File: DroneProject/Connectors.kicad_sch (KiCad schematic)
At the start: 7 parts, among them J21 Battery, J22 Debug, J23 UART, J24 Screw_Terminal_01x03, J25 Screw_Terminal_01x03, J26 Screw_Terminal_01x03, J27 Screw_Terminal_01x03

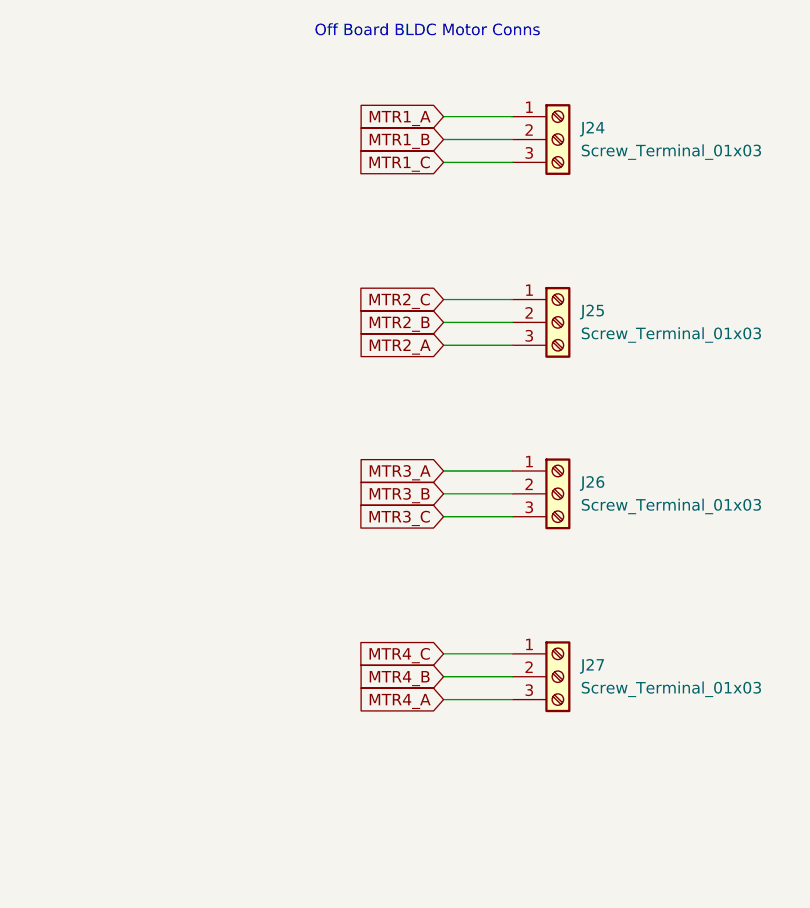
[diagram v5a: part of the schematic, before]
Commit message: Removed C1 and motor controllers from main platform and moved to own project
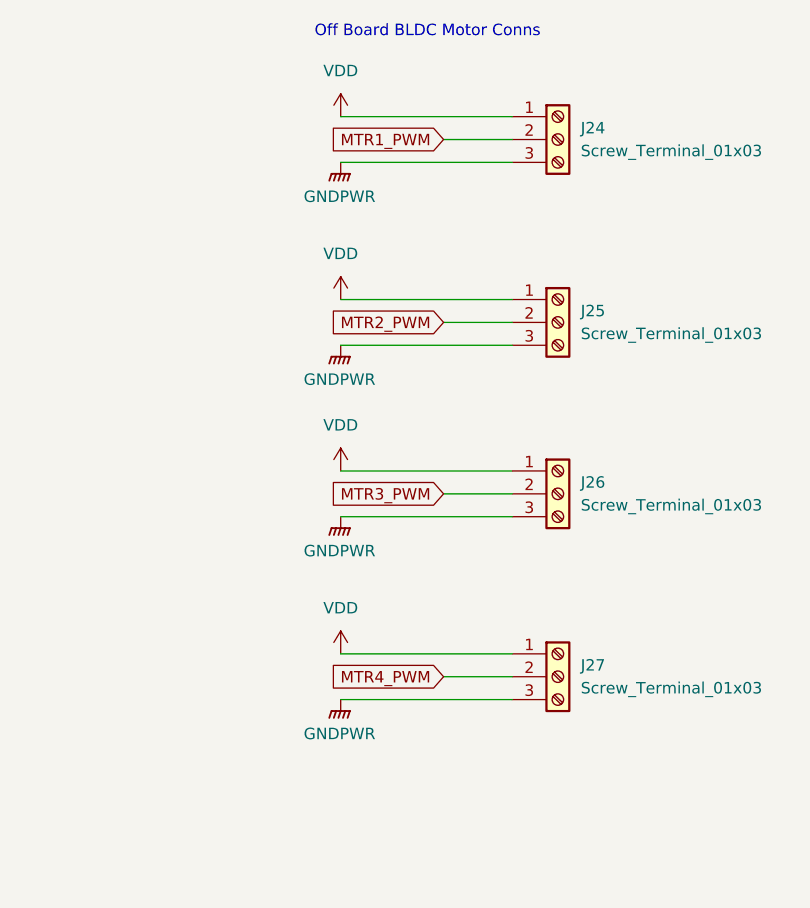
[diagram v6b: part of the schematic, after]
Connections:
- net MTR2_A is gone; now on net GNDPWR: J25.3 (Pin_3)
- net MTR2_C is gone; now on net VDD: J25.1 (Pin_1)
- net MTR3_A is gone; now on net VDD: J26.1 (Pin_1)
- net MTR3_C is gone; now on net GNDPWR: J26.3 (Pin_3)
- net MTR4_A is gone; now on net GNDPWR: J27.3 (Pin_3)
- net MTR4_C is gone; now on net VDD: J27.1 (Pin_1)
- net MTR1_A renamed VDD
- net MTR1_B renamed MTR1_PWM
- net MTR1_C renamed GNDPWR
- net MTR2_B renamed MTR2_PWM
- net MTR3_B renamed MTR3_PWM
- net MTR4_B renamed MTR4_PWM

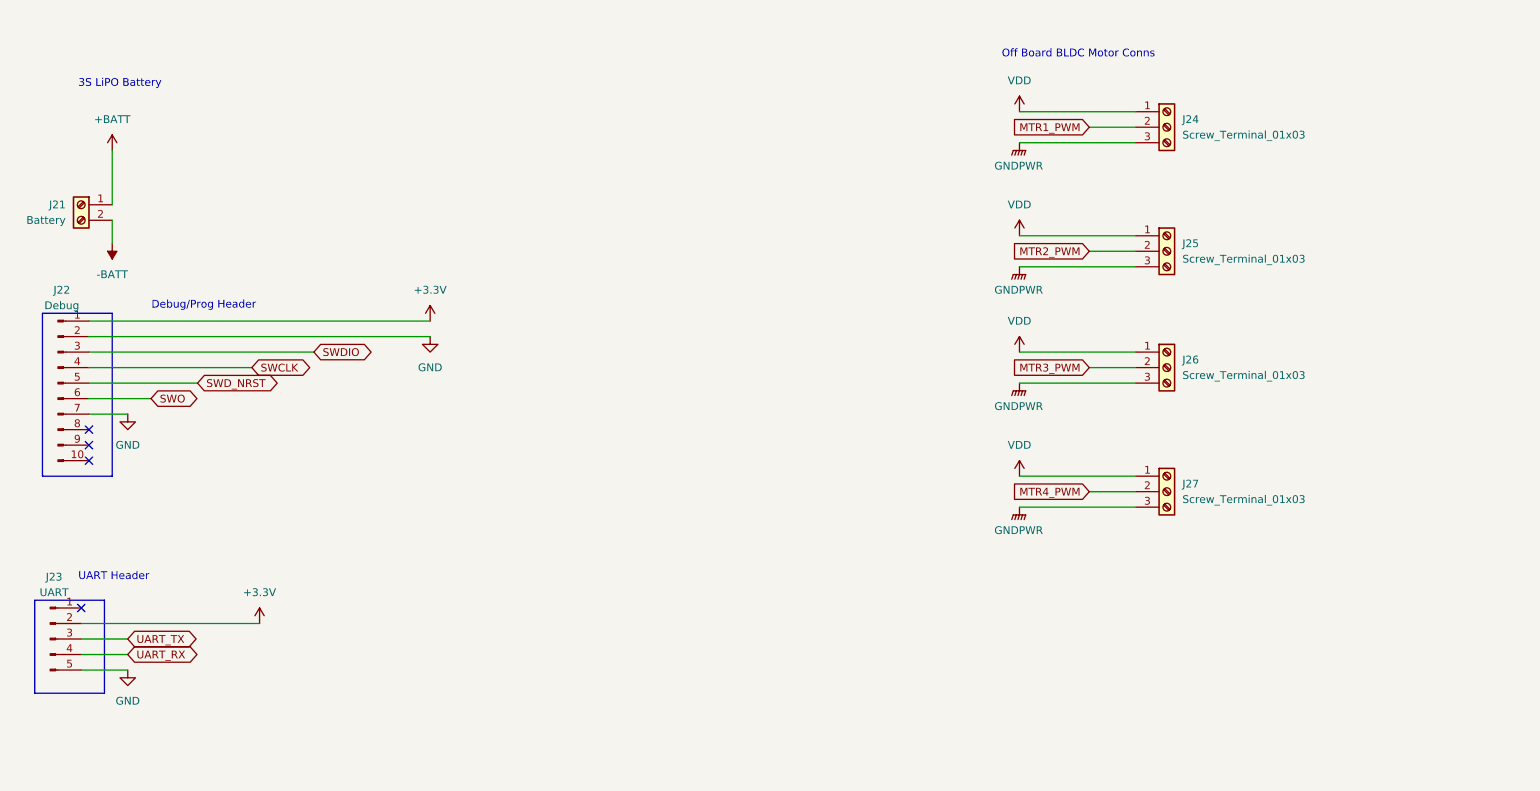
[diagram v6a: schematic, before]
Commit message: Completed schematic for brushless ESC and added needed components to main board.  The plan is to mount the ESCs on the main board using 2.54mm Vert Conn Headers
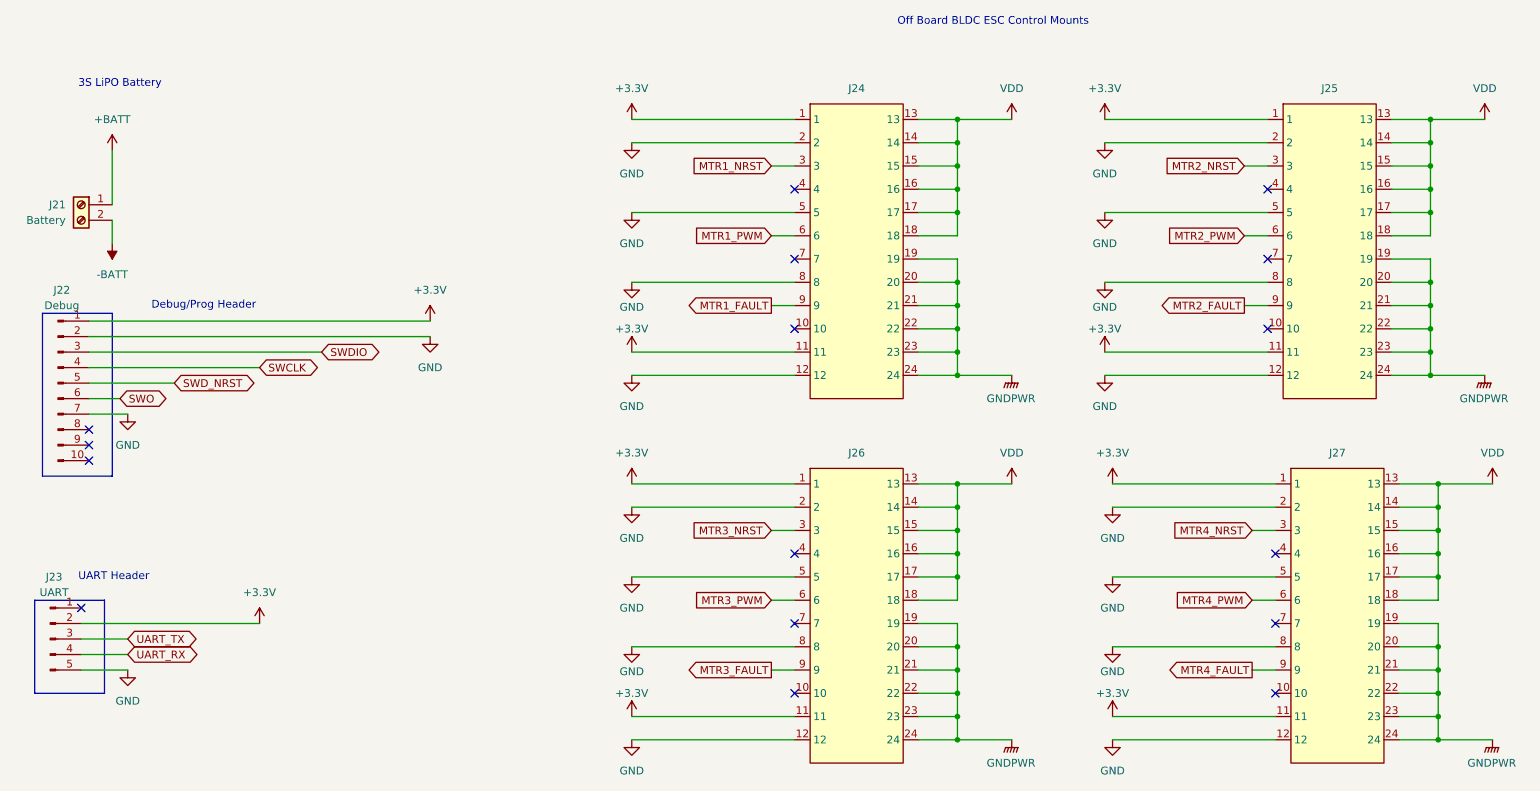
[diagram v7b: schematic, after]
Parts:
- removed J24, J25, J26, J27: Screw_Terminal_01x03, Library:CUI_TB005_-762-03BE, symbol Connector:Screw_Terminal_01x03
- added J24, J25, J26, J27: ~, Library:BrushlessESC, symbol Global:BrushlessESC
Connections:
- net +3.3V: now also J24.1, J24.11, J25.1, J25.11, J26.1, J26.11, J27.1, J27.11
- net GND: now also J24.12, J24.2, J24.5, J24.8, J25.12, J25.2, J25.5, J25.8, J26.12, J26.2, J26.5, J26.8, J27.12, J27.2, J27.5, J27.8
- net GNDPWR: now also J24.19, J24.20, J24.21, J24.22, J24.23, J24.24, J25.19, J25.20, J25.21, J25.22, J25.23, J25.24, J26.19, J26.20, J26.21, J26.22, J26.23, J26.24, J27.19, J27.20, J27.21, J27.22, J27.23, J27.24
- net MTR1_PWM: now also J24.6
- net MTR2_PWM: now also J25.6
- net MTR3_PWM: now also J26.6
- net MTR4_PWM: now also J27.6
- net VDD: now also J24.13, J24.14, J24.15, J24.16, J24.17, J24.18, J25.13, J25.14, J25.15, J25.16, J25.17, J25.18, J26.13, J26.14, J26.15, J26.16, J26.17, J26.18, J27.13, J27.14, J27.15, J27.16, J27.17, J27.18
- new net MTR1_FAULT: J24.9
- new net MTR1_NRST: J24.3
- new net MTR2_FAULT: J25.9
- new net MTR2_NRST: J25.3
- new net MTR3_FAULT: J26.9
- new net MTR3_NRST: J26.3
- new net MTR4_FAULT: J27.9
- new net MTR4_NRST: J27.3
- no-connect marks 4 -> 16
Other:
- note added: "Off Board BLDC ESC Control Mounts"
- note removed: "Off Board BLDC Motor Conns"

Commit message: Finished layout for controller board
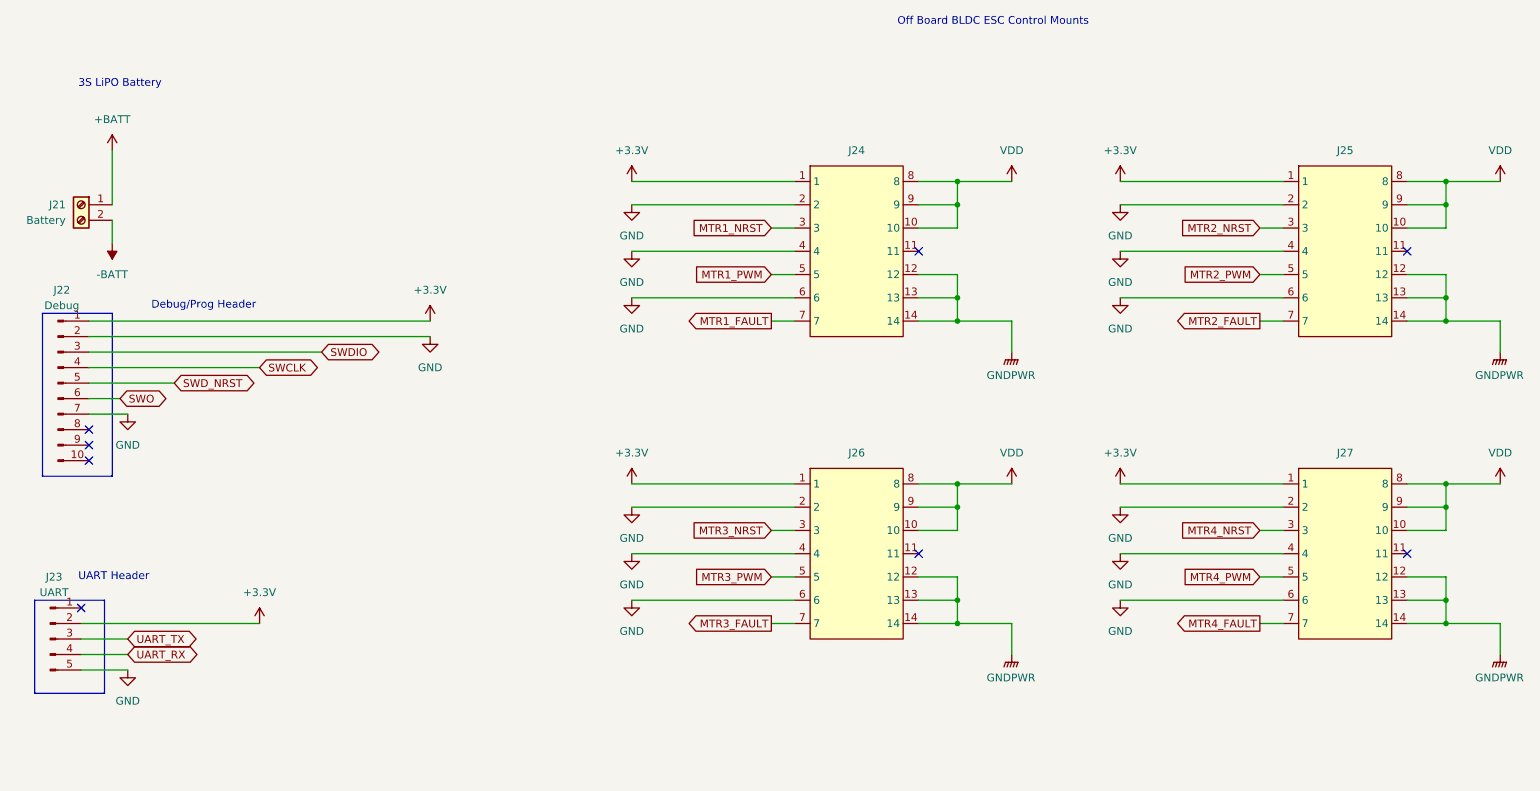
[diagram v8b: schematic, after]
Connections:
- net +3.3V: no longer J24.11, J25.11, J26.11, J27.11
- net GND: now also J24.4, J24.6, J25.4, J25.6, J26.4, J26.6, J27.4, J27.6; no longer J24.12, J24.5, J24.8, J25.12, J25.5, J25.8, J26.12, J26.5, J26.8, J27.12, J27.5, J27.8
- net GNDPWR: now also J24.12, J24.13, J24.14, J25.12, J25.13, J25.14, J26.12, J26.13, J26.14, J27.12, J27.13, J27.14; no longer J24.19, J24.20, J24.21, J24.22, J24.23, J24.24, J25.19, J25.20, J25.21, J25.22, J25.23, J25.24, J26.19, J26.20, J26.21, J26.22, J26.23, J26.24, J27.19, J27.20, J27.21, J27.22, J27.23, J27.24
- net MTR1_FAULT: now also J24.7; no longer J24.9
- net MTR1_PWM: now also J24.5; no longer J24.6
- net MTR2_FAULT: now also J25.7; no longer J25.9
- net MTR2_PWM: now also J25.5; no longer J25.6
- net MTR3_FAULT: now also J26.7; no longer J26.9
- net MTR3_PWM: now also J26.5; no longer J26.6
- net MTR4_FAULT: now also J27.7; no longer J27.9
- net MTR4_PWM: now also J27.5; no longer J27.6
- net VDD: now also J24.10, J24.8, J24.9, J25.10, J25.8, J25.9, J26.10, J26.8, J26.9, J27.10, J27.8, J27.9; no longer J24.13, J24.14, J24.15, J24.16, J24.17, J24.18, J25.13, J25.14, J25.15, J25.16, J25.17, J25.18, J26.13, J26.14, J26.15, J26.16, J26.17, J26.18, J27.13, J27.14, J27.15, J27.16, J27.17, J27.18
- no-connect marks 16 -> 8
